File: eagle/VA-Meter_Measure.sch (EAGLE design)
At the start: 10 parts, among them IC1 MEGA328P

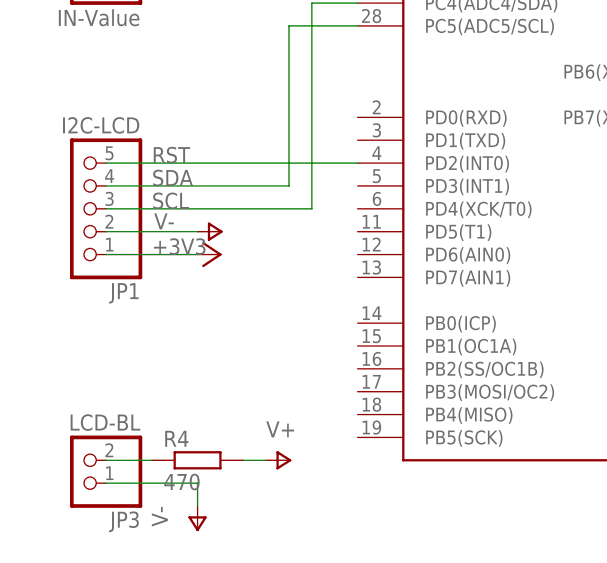
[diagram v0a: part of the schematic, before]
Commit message: VA-Meter_Measure 回路図、SCLとSDAの信号線の名前が逆だったのを修正
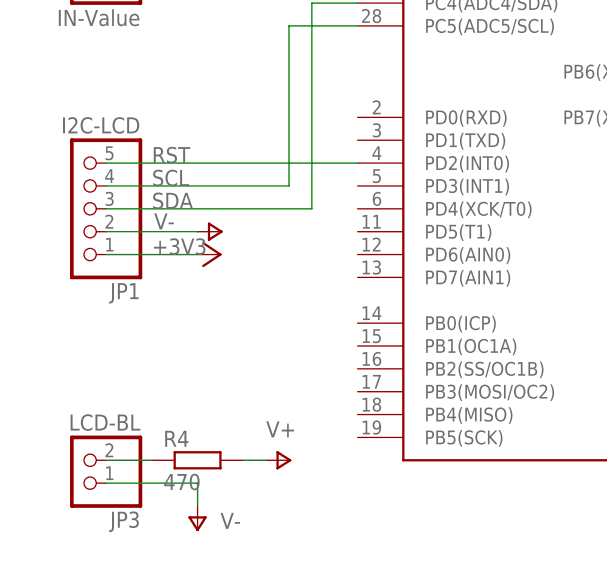
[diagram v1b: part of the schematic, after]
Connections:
- net SCL: now also IC1.PC5(ADC5/SCL), JP1.4; no longer IC1.PC4(ADC4/SDA), JP1.3
- net SDA: now also IC1.PC4(ADC4/SDA), JP1.3; no longer IC1.PC5(ADC5/SCL), JP1.4
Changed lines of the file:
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@@
 <setting verticaltext="up"/>
 </settings>
-<grid distance="0.1" unitdist="inch" unit="inch" style="dots" multiple="1" display="yes" altdistance="0.01" altunitdist="inch" altunit="inch"/>
+<grid distance="0.1" unitdist="inch" unit="inch" style="lines" multiple="1" display="no" altdistance="0.01" altunitdist="inch" altunit="inch"/>
 <layers>
 <layer number="1" name="Top" color="4" fill="1" visible="no" active="no"/>
@@
 <instance part="R4" gate="G$1" x="83.82" y="55.88"/>
 <instance part="P+1" gate="1" x="93.98" y="55.88" rot="R270"/>
-<instance part="P-6" gate="1" x="83.82" y="48.26"/>
+<instance part="P-6" gate="1" x="83.82" y="48.26" smashed="yes">
+<attribute name="VALUE" x="86.36" y="48.26" size="1.778" layer="96"/>
+</instance>
 <instance part="C5" gate="G$1" x="162.56" y="109.22" smashed="yes" rot="R270">
 <attribute name="NAME" x="162.941" y="107.696" size="1.778" layer="95" rot="R270"/>
@@
 </segment>
 </net>
-<net name="SCL" class="0">
+<net name="SDA" class="0">
 <segment>
 <wire x1="73.66" y1="83.82" x2="96.52" y2="83.82" width="0.1524" layer="91"/>
@@
 </segment>
 </net>
-<net name="SDA" class="0">
+<net name="SCL" class="0">
 <segment>
 <wire x1="73.66" y1="86.36" x2="93.98" y2="86.36" width="0.1524" layer="91"/>

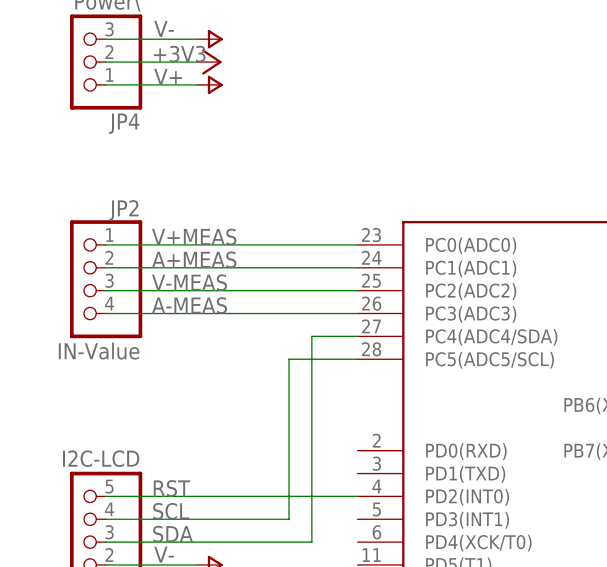
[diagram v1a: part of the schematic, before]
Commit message: VA-Meter_Measure.sch デジタル部回路図修正 入力端子名の変更
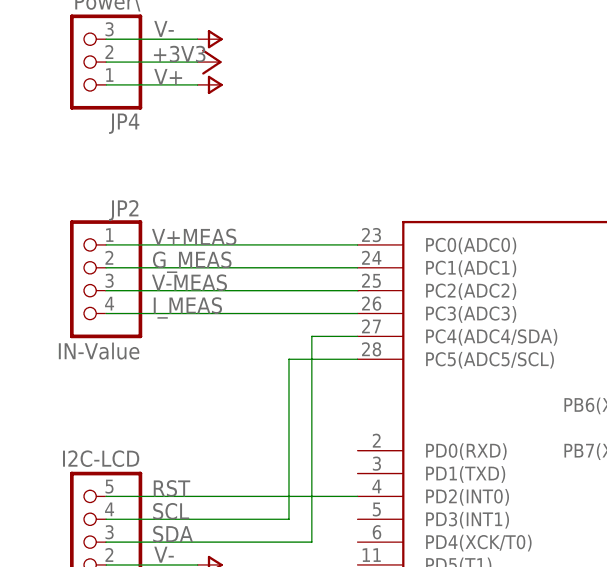
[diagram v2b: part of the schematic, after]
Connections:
- net A+MEAS renamed G_MEAS
- net A-MEAS renamed I_MEAS
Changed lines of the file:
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@@
 <?xml version="1.0" encoding="utf-8"?>
 <!DOCTYPE eagle SYSTEM "eagle.dtd">
-<eagle version="6.6.0">
+<eagle version="7.1.0">
 <drawing>
 <settings>
@@
 </segment>
 </net>
-<net name="A+MEAS" class="0">
+<net name="G_MEAS" class="0">
 <segment>
 <pinref part="JP2" gate="A" pin="2"/>
@@
 </segment>
 </net>
-<net name="A-MEAS" class="0">
+<net name="I_MEAS" class="0">
 <segment>
 <pinref part="IC1" gate="G$1" pin="PC3(ADC3)"/>
